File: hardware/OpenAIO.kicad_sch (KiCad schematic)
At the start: 4 parts, among them U24 AIO_outline, U25 INA186A3IDCKR

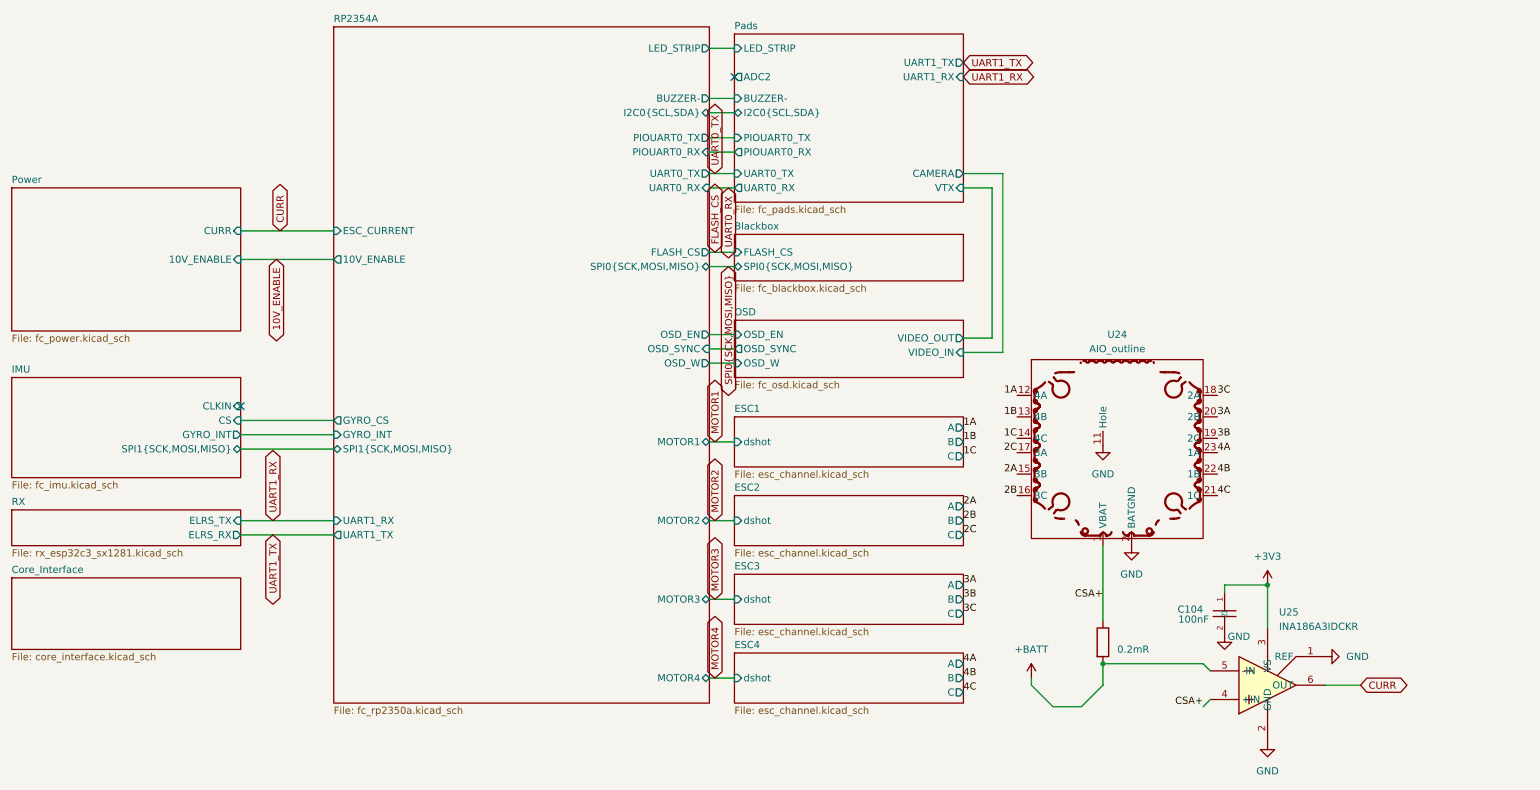
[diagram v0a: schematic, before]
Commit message: OpenAIO: test points TP10-TP30 as LGA position markers (schematic + Base), project files as re-saved by KiCad
Co-Authored-By: Claude Fable 5 <noreply@anthropic.com>
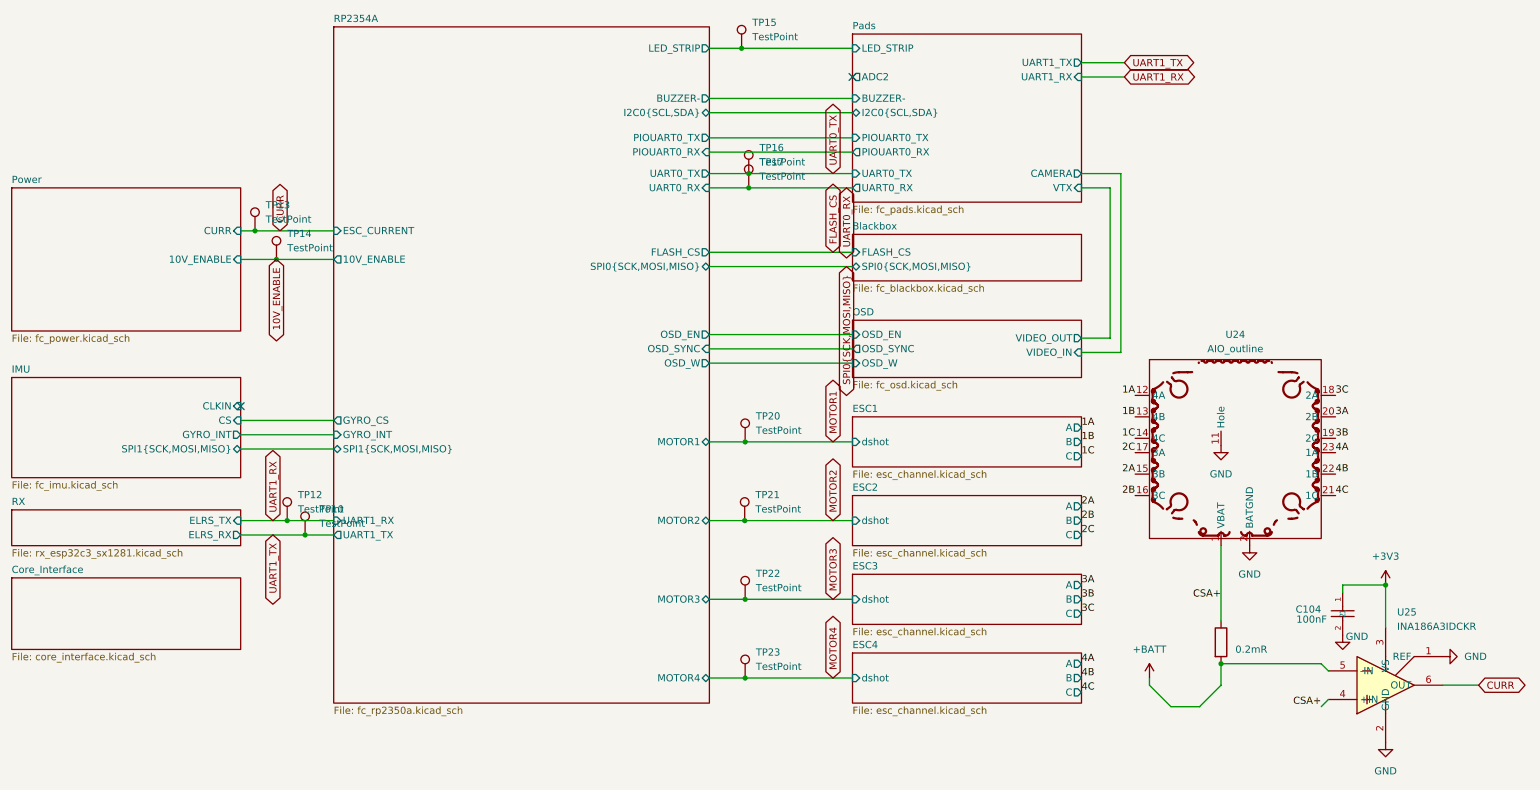
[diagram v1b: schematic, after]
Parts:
- added TP10: TestPoint, OpenDrone:TestPoint_Pad_D1.0mm, symbol Connector:TestPoint
- added TP12, TP13, TP14, TP15, TP16, TP17, TP20, TP21, TP22, TP23: TestPoint, TestPoint:TestPoint_Pad_D1.0mm, symbol Connector:TestPoint
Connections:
- net 10V_ENABLE: now also TP14.1
- net CURR: now also TP13.1
- net MOTOR1: now also TP20.1
- net MOTOR2: now also TP21.1
- net MOTOR3: now also TP22.1
- net MOTOR4: now also TP23.1
- net Pads/LED_STRIP: now also TP15.1
- net UART0_RX: now also TP17.1
- net UART0_TX: now also TP16.1
- net UART1_RX: now also TP12.1
- net UART1_TX: now also TP10.1
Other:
- moved on the sheet: C104, U24, U25

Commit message: OpenAIO: LGA pins from Stan's marker test points, 30 pads, J90/J91 regenerated and placed
lga_gen.py --from-base reads the marker test points on the Base (position +
net) into its pin table and generates footprints, symbol and interface
sheet; lga_apply.py replaces the markers with J90 at the pattern centre and
J91 on the Core, marks the marker symbols exclude-from-board and adds the
LED_STRIP global label on the root (it now crosses the LGA). Plugin update
assigned all 30 pad nets on both boards.

Co-Authored-By: Claude Fable 5 <noreply@anthropic.com>
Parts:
- removed TP10: TestPoint, OpenDrone:TestPoint_Pad_D1.0mm, symbol Connector:TestPoint
- added TP41: TestPoint, TestPoint:TestPoint_Pad_D1.0mm, symbol Connector:TestPoint
- TP12, TP13, TP14, TP15, TP16, TP17, TP20, TP21, TP22, TP23: now left out of the parts list
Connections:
- net UART1_TX: now also TP41.1
- net Pads/LED_STRIP renamed LED_STRIP
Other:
- moved on the sheet: TP12
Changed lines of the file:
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@@
 	)
 	(junction
+		(at 72.39 110.49)
+		(diameter 0)
+		(color 0 0 0 0)
+	)
+	(junction
 		(at 152.4 48.895)
 		(diameter 0)
@@
 	)
 	(junction
-		(at 70.485 107.95)
-		(diameter 0)
-		(color 0 0 0 0)
-	)
-	(junction
 		(at 265.43 119.38)
 		(diameter 0)
@@
 	)
 	(junction
-		(at 73.66 110.49)
+		(at 151.765 93.98)
 		(diameter 0)
 		(color 0 0 0 0)
 	)
 	(junction
-		(at 151.765 93.98)
+		(at 70.485 107.95)
 		(diameter 0)
 		(color 0 0 0 0)
@@
 	(wire
 		(pts
+			(xy 72.39 110.49) (xy 78.74 110.49)
+		)
+		(stroke
+			(width 0)
+			(type default)
+		)
+	)
+	(wire
+		(pts
 			(xy 151.765 93.98) (xy 170.815 93.98)
 		)
@@
 	(wire
 		(pts
-			(xy 73.66 110.49) (xy 78.74 110.49)
+			(xy 62.23 110.49) (xy 72.39 110.49)
 		)
 		(stroke
@@
 	(wire
 		(pts
-			(xy 62.23 110.49) (xy 73.66 110.49)
+			(xy 145.415 40.005) (xy 170.815 40.005)
 		)
 		(stroke
@@
 	(wire
 		(pts
-			(xy 145.415 40.005) (xy 170.815 40.005)
+			(xy 223.52 135.89) (xy 223.52 137.16)
 		)
 		(stroke
@@
 	(wire
 		(pts
-			(xy 223.52 135.89) (xy 223.52 137.16)
+			(xy 145.415 121.92) (xy 151.765 121.92)
 		)
 		(stroke
@@
 	(wire
 		(pts
-			(xy 145.415 121.92) (xy 151.765 121.92)
+			(xy 145.415 107.95) (xy 151.6832 107.95)
 		)
 		(stroke
@@
 	(wire
 		(pts
-			(xy 145.415 107.95) (xy 151.6832 107.95)
+			(xy 151.13 24.13) (xy 170.815 24.13)
 		)
 		(stroke
@@
 	(wire
 		(pts
-			(xy 151.13 24.13) (xy 170.815 24.13)
+			(xy 145.415 93.98) (xy 151.765 93.98)
 		)
 		(stroke
@@
 	(wire
 		(pts
-			(xy 145.415 93.98) (xy 151.765 93.98)
+			(xy 145.415 77.47) (xy 170.815 77.47)
 		)
 		(stroke
@@
 	(wire
 		(pts
-			(xy 145.415 77.47) (xy 170.815 77.47)
+			(xy 70.485 104.14) (xy 70.485 107.95)
 		)
 		(stroke
@@
 		(body_style 1)
 		(exclude_from_sim no)
-		(in_bom yes)
-		(on_board yes)
+		(in_bom no)
+		(on_board no)
 		(in_pos_files yes)
 		(dnp no)
@@
 		(body_style 1)
 		(exclude_from_sim no)
-		(in_bom yes)
-		(on_board yes)
+		(in_bom no)
+		(on_board no)
 		(in_pos_files yes)
 		(dnp no)
@@
 		(body_style 1)
 		(exclude_from_sim no)
-		(in_bom yes)
-		(on_board yes)
+		(in_bom no)
+		(on_board no)
 		(in_pos_files yes)
 		(dnp no)
@@
 		(body_style 1)
 		(exclude_from_sim no)
-		(in_bom yes)
-		(on_board yes)
+		(in_bom no)
+		(on_board no)
 		(in_pos_files yes)
 		(dnp no)
@@
 	)
 	(symbol
+		(lib_id "Connector:TestPoint")
+		(at 72.39 110.49 0)
+		(unit 1)
+		(body_style 1)
+		(exclude_from_sim no)
+		(in_bom no)
+		(on_board no)
+		(in_pos_files yes)
+		(dnp no)
+		(fields_autoplaced yes)
+		(property "Reference" "TP41"
+			(at 74.295 105.9179 0)
+			(show_name no)
+			(do_not_autoplace no)
+			(effects
+				(font
+					(size 1.27 1.27)
+				)
+				(justify left)
+			)
+		)
+		(property "Value" "TestPoint"
+			(at 74.295 108.4579 0)
+			(show_name no)
+			(do_not_autoplace no)
+			(effects
+				(font
+					(size 1.27 1.27)
+				)
+				(justify left)
+			)
+		)
+		(property "Footprint" "TestPoint:TestPoint_Pad_D1.0mm"
+			(at 77.47 110.49 0)
+			(hide yes)
+			(show_name no)
+			(do_not_autoplace no)
+			(effects
+				(font
+					(size 1.27 1.27)
+				)
+			)
+		)
+		(property "Datasheet" ""
+			(at 77.47 110.49 0)
+			(hide yes)
+			(show_name no)
+			(do_not_autoplace no)
+			(effects
+				(font
+					(size 1.27 1.27)
+				)
+			)
+		)
+		(property "Description" "test point"
+			(at 72.39 110.49 0)
+			(hide yes)
+			(show_name no)
+			(do_not_autoplace no)
+			(effects
+				(font
+					(size 1.27 1.27)
+				)
+			)
+		)
+		(pin "1"
+		)
+		(instances
+			(project "OpenAIO-Base"
+				(path "/fb88b6f9-ee39-4640-a9d4-04a17ceeac64"
+					(reference "TP41")
+					(unit 1)
+				)
+			)
+		)
+	)
+	(symbol
 		(lib_id "ESCLibrary:GRM033R61C104KE84D")
 		(at 257.81 124.46 270)
@@
 	(symbol
 		(lib_id "Connector:TestPoint")
-		(at 70.485 107.95 0)
+		(at 70.485 104.14 0)
 		(unit 1)
 		(body_style 1)
 		(exclude_from_sim no)
-		(in_bom yes)
-		(on_board yes)
+		(in_bom no)
+		(on_board no)
 		(in_pos_files yes)
 		(dnp no)
 		(fields_autoplaced yes)
 		(property "Reference" "TP12"
-			(at 72.39 103.3779 0)
+			(at 72.39 99.5679 0)
 			(show_name no)
 			(do_not_autoplace no)
@@
 		)
 		(property "Value" "TestPoint"
-			(at 72.39 105.9179 0)
+			(at 72.39 102.1079 0)
 			(show_name no)
 			(do_not_autoplace no)
@@
 		)
 		(property "Footprint" "TestPoint:TestPoint_Pad_D1.0mm"
-			(at 75.565 107.95 0)
+			(at 75.565 104.14 0)
 			(hide yes)
 			(show_name no)
@@
 		)
 		(property "Datasheet" ""
-			(at 75.565 107.95 0)
+			(at 75.565 104.14 0)
 			(hide yes)
 			(show_name no)
@@
 		)
 		(property "Description" "test point"
-			(at 70.485 107.95 0)
+			(at 70.485 104.14 0)
 			(hide yes)
 			(show_name no)
@@
 		(body_style 1)
 		(exclude_from_sim no)
-		(in_bom yes)
-		(on_board yes)
+		(in_bom no)
+		(on_board no)
 		(in_pos_files yes)
 		(dnp no)
@@
 		(body_style 1)
 		(exclude_from_sim no)
-		(in_bom yes)
-		(on_board yes)
+		(in_bom no)
+		(on_board no)
 		(in_pos_files yes)
 		(dnp no)
@@
 	)
 	(symbol
-		(lib_id "Connector:TestPoint")
-		(at 73.66 110.49 0)
-		(unit 1)
-		(body_style 1)
-		(exclude_from_sim no)
-		(in_bom yes)
-		(on_board yes)
-		(in_pos_files yes)
-		(dnp no)
-		(fields_autoplaced yes)
-		(property "Reference" "TP10"
-			(at 76.2 105.9179 0)
-			(show_name no)
-			(do_not_autoplace no)
-			(effects
-				(font
-					(size 1.27 1.27)
-				)
-				(justify left)
-			)
-		)
-		(property "Value" "TestPoint"
-			(at 76.2 108.4579 0)
-			(show_name no)
-			(do_not_autoplace no)
-			(effects
-				(font
-					(size 1.27 1.27)
-				)
-				(justify left)
-			)
-		)
-		(property "Footprint" "OpenDrone:TestPoint_Pad_D1.0mm"
-			(at 78.74 110.49 0)
-			(hide yes)
-			(show_name no)
-			(do_not_autoplace no)
-			(effects
-				(font
-					(size 1.27 1.27)
-				)
-			)
-		)
-		(property "Datasheet" ""
-			(at 78.74 110.49 0)
-			(hide yes)
-			(show_name no)
-			(do_not_autoplace no)
-			(effects
-				(font
-					(size 1.27 1.27)
-				)
-			)
-		)
-		(property "Description" "test point"
-			(at 73.66 110.49 0)
-			(hide yes)
-			(show_name no)
-			(do_not_autoplace no)
-			(effects
-				(font
-					(size 1.27 1.27)
-				)
-			)
-		)
-		(pin "1"
-		)
-		(instances
-			(project "OpenAIO-Base"
-				(path "/fb88b6f9-ee39-4640-a9d4-04a17ceeac64"
-					(reference "TP10")
-					(unit 1)
-				)
-			)
-		)
-	)
-	(symbol
 		(lib_id "power:GND")
 		(at 241.3 112.395 0)
@@
 		(body_style 1)
 		(exclude_from_sim no)
-		(in_bom yes)
-		(on_board yes)
+		(in_bom no)
+		(on_board no)
 		(in_pos_files yes)
 		(dnp no)
@@
 		(body_style 1)
 		(exclude_from_sim no)
-		(in_bom yes)
-		(on_board yes)
+		(in_bom no)
+		(on_board no)
 		(in_pos_files yes)
 		(dnp no)
@@
 		(body_style 1)
 		(exclude_from_sim no)
-		(in_bom yes)
-		(on_board yes)
+		(in_bom no)
+		(on_board no)
 		(in_pos_files yes)
 		(dnp no)
@@
 		)
 	)
+	(global_label "LED_STRIP"
+		(shape bidirectional)
+		(at 160.02 24.13 0)
+		(effects
+			(font
+				(size 1.27 1.27)
+			)
+			(justify left)
+		)
+	)

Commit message: OpenAIO: new marker test points TP29 (BUZZER-) and TP30 (+5V) on the Base; lga_apply only excludes the markers it consumed
Co-Authored-By: Claude Fable 5 <noreply@anthropic.com>
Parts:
- added TP29: TestPoint, TestPoint:TestPoint_Pad_D1.0mm, symbol Connector:TestPoint
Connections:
- net Pads/BUZZER-: now also TP29.1
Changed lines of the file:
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@@
 		(color 0 0 0 0)
 	)
+	(junction
+		(at 150.495 33.02)
+		(diameter 0)
+		(color 0 0 0 0)
+	)
 	(no_connect
 		(at 62.23 87.63)
@@
 	(wire
 		(pts
-			(xy 145.415 33.02) (xy 170.815 33.02)
+			(xy 145.415 33.02) (xy 150.495 33.02)
 		)
 		(stroke
@@
 	(wire
 		(pts
+			(xy 150.495 33.02) (xy 170.815 33.02)
+		)
+		(stroke
+			(width 0)
+			(type default)
+		)
+	)
+	(wire
+		(pts
 			(xy 211.455 46.355) (xy 218.44 46.355)
 		)
@@
 		)
 	)
+	(global_label "LED_STRIP"
+		(shape bidirectional)
+		(at 160.02 24.13 0)
+		(effects
+			(font
+				(size 1.27 1.27)
+			)
+			(justify left)
+		)
+		(property "Intersheetrefs" "${INTERSHEET_REFS}"
+			(at 160.02 24.13 0)
+			(hide yes)
+			(show_name no)
+			(do_not_autoplace no)
+			(effects
+				(font
+					(size 1.27 1.27)
+				)
+			)
+		)
+	)
 	(global_label "UART0_TX"
 		(shape bidirectional)
@@
 	(symbol
 		(lib_id "Connector:TestPoint")
+		(at 150.495 33.02 0)
+		(unit 1)
+		(body_style 1)
+		(exclude_from_sim no)
+		(in_bom no)
+		(on_board yes)
+		(in_pos_files yes)
+		(dnp no)
+		(fields_autoplaced yes)
+		(property "Reference" "TP29"
+			(at 152.4 28.4479 0)
+			(show_name no)
+			(do_not_autoplace no)
+			(effects
+				(font
+					(size 1.27 1.27)
+				)
+				(justify left)
+			)
+		)
+		(property "Value" "TestPoint"
+			(at 152.4 30.9879 0)
+			(show_name no)
+			(do_not_autoplace no)
+			(effects
+				(font
+					(size 1.27 1.27)
+				)
+				(justify left)
+			)
+		)
+		(property "Footprint" "TestPoint:TestPoint_Pad_D1.0mm"
+			(at 155.575 33.02 0)
+			(hide yes)
+			(show_name no)
+			(do_not_autoplace no)
+			(effects
+				(font
+					(size 1.27 1.27)
+				)
+			)
+		)
+		(property "Datasheet" ""
+			(at 155.575 33.02 0)
+			(hide yes)
+			(show_name no)
+			(do_not_autoplace no)
+			(effects
+				(font
+					(size 1.27 1.27)
+				)
+			)
+		)
+		(property "Description" "test point"
+			(at 150.495 33.02 0)
+			(hide yes)
+			(show_name no)
+			(do_not_autoplace no)
+			(effects
+				(font
+					(size 1.27 1.27)
+				)
+			)
+		)
+		(pin "1"
+		)
+		(instances
+			(project "OpenAIO-Base"
+				(path "/fb88b6f9-ee39-4640-a9d4-04a17ceeac64"
+					(reference "TP29")
+					(unit 1)
+				)
+			)
+		)
+	)
+	(symbol
+		(lib_id "Connector:TestPoint")
 		(at 152.4 46.355 0)
 		(unit 1)
@@
 		)
 	)
-	(global_label "LED_STRIP"
-		(shape bidirectional)
-		(at 160.02 24.13 0)
-		(effects
-			(font
-				(size 1.27 1.27)
-			)
-			(justify left)
-		)
-	)

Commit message: OpenAIO: LGA 31 pins (+5V and BUZZER- added, stray GND removed), J91 follows the pattern centre automatically
Co-Authored-By: Claude Fable 5 <noreply@anthropic.com>
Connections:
- net Pads/BUZZER- renamed BUZZER-
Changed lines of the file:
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@@
 		(exclude_from_sim no)
 		(in_bom no)
-		(on_board yes)
+		(on_board no)
 		(in_pos_files yes)
 		(dnp no)
@@
 		)
 	)
+	(global_label "BUZZER-"
+		(shape bidirectional)
+		(at 160.02 33.02 0)
+		(effects
+			(font
+				(size 1.27 1.27)
+			)
+			(justify left)
+		)
+	)
